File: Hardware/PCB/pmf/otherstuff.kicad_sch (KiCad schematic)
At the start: 65 parts, among them J10 Synth_power_2x5, J11 Conn_02x07_Odd_Even, J12 AudioJack2, J13 Conn_02x07_Odd_Even, J14 Conn_02x07_Odd_Even, J5 AudioJack2, J6 AudioJack2, J7 AudioJack2, J8 AudioJack2, J9 AudioJack2, SW1 SW_Rotary12, U2 TL072

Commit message: Rename libraries
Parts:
- C10, C11: footprint ao_tht:CP_Radial_D6.3mm_P2.50mm -> AO_tht:CP_Radial_D6.3mm_P2.50mm; symbol ao_symbols:CP -> AO_symbols:CP
- C12, C13: footprint ao_tht:C_Disc_D3.0mm_W1.6mm_P2.50mm -> AO_tht:C_Disc_D3.0mm_W1.6mm_P2.50mm; symbol ao_symbols:C -> AO_symbols:C
- D1, D2: footprint ao_tht:D_DO-41_SOD81_P10.16mm_Horizontal -> AO_tht:D_DO-41_SOD81_P10.16mm_Horizontal; symbol ao_symbols:1N5817 -> AO_symbols:1N5817
- GRAF1, GRAF2: symbol ao_symbols:Graphic -> AO_symbols:Graphic
- GRAF3: footprint ao_tht:analogoutput -> AO_tht:analogoutput; symbol ao_symbols:Graphic -> AO_symbols:Graphic
- H1, H2, H3: footprint ao_tht:MountingHole_3.2mm_M3 -> AO_tht:MountingHole_3.2mm_M3; symbol ao_symbols:MountingHole -> AO_symbols:MountingHole
- J10: footprint ao_tht:Power_Header -> AO_tht:Power_Header; symbol ao_symbols:Synth_power_2x5 -> AO_symbols:Synth_power_2x5
- J12, J5, J6, J7, J8, J9: footprint ao_tht:Jack_6.35mm_PJ_629HAN_slots -> AO_tht:Jack_6.35mm_PJ_629HAN_slots; symbol ao_symbols:AudioJack2 -> AO_symbols:AudioJack2
- R21, R22, R23, R24, R25, R26, R27, R28, R29, R31, R33, R34, R35, R36, R37, R38, R40, R42, R43, R47, R48, R49, R50, R51, R55, R56, R57, R58: footprint ao_tht:R_Axial_DIN0207_L6.3mm_D2.5mm_P10.16mm_Horizontal -> AO_tht:R_Axial_DIN0207_L6.3mm_D2.5mm_P10.16mm_Horizontal; symbol ao_symbols:R -> AO_symbols:R
- R30, R32, R39, R41, R44, R45, R46, R52, R53, R54: symbol ao_symbols:R -> AO_symbols:R
- SW1: footprint ao_tht:Rotary_Switch -> AO_tht:Rotary_Switch; symbol ao_symbols:SW_Rotary12 -> AO_symbols:SW_Rotary12
- TP7, TP8, TP9: footprint ao_tht:TestPoint_THTPad_D1.5mm_Drill0.7mm -> AO_tht:TestPoint_THTPad_D1.5mm_Drill0.7mm; symbol ao_symbols:TestPoint -> AO_symbols:TestPoint
- U2: footprint ao_tht:DIP-8_W7.62mm_Socket_LongPads -> AO_tht:DIP-8_W7.62mm_Socket_LongPads; symbol ao_symbols:TL072 -> AO_symbols:TL072

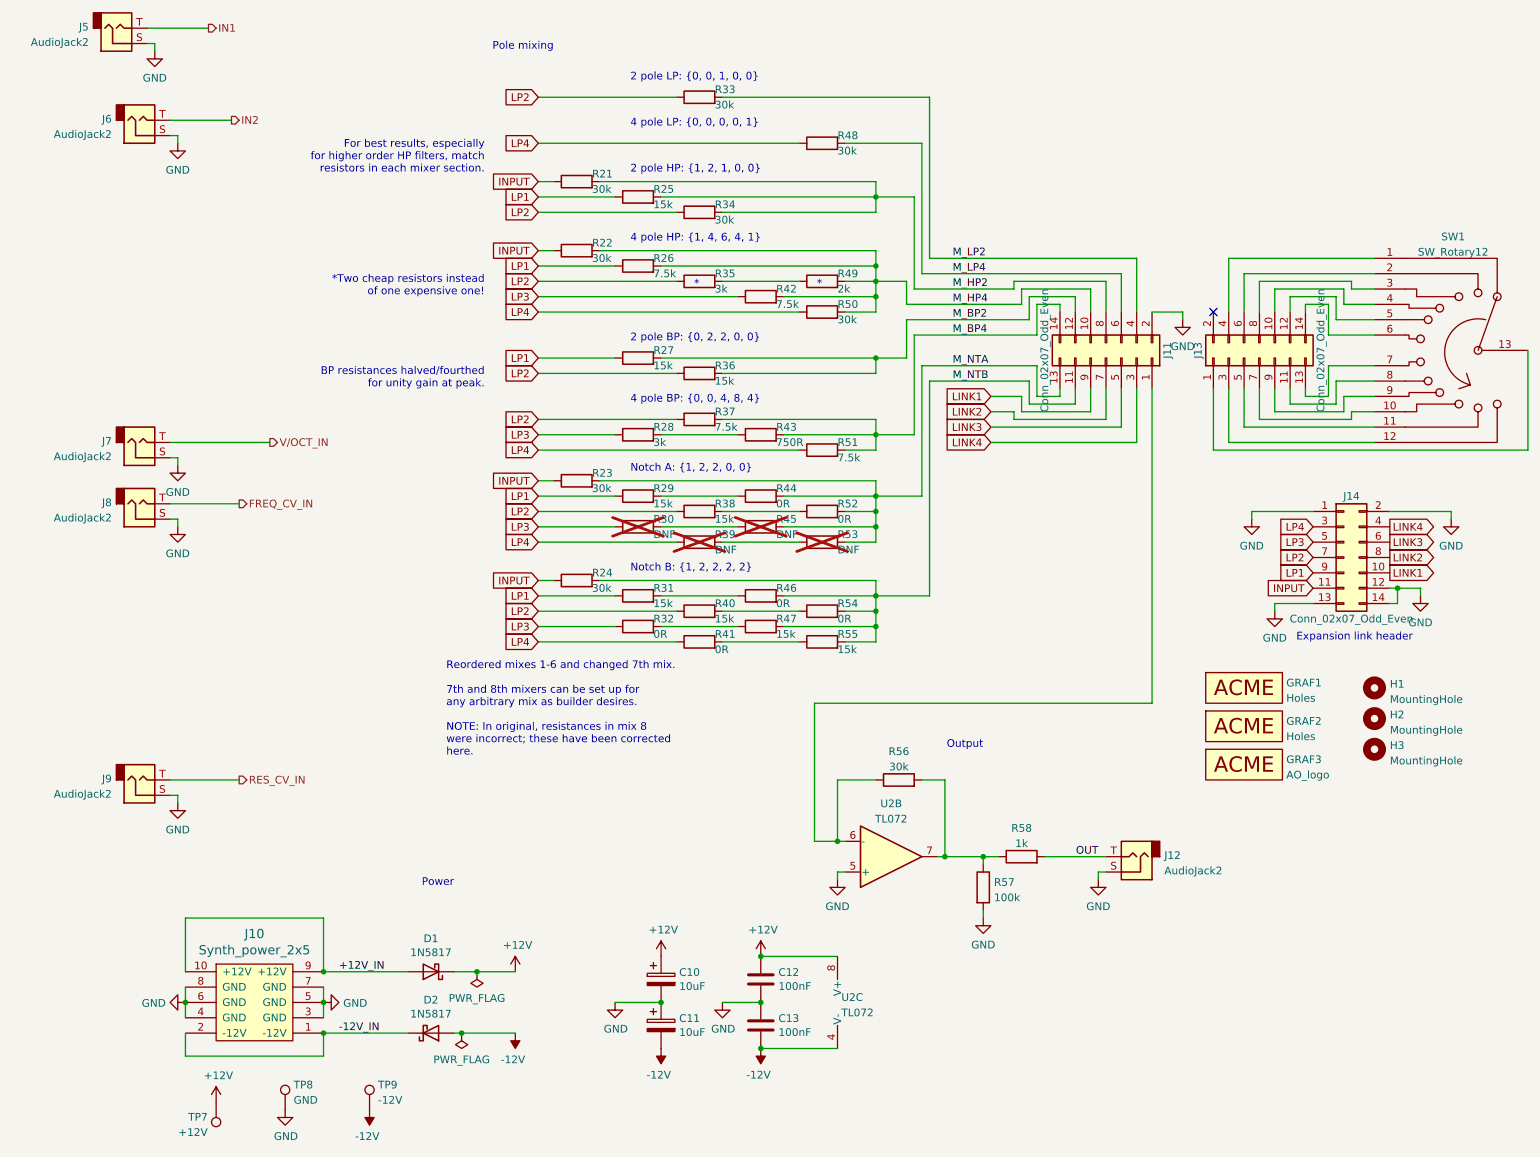
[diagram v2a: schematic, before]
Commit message: Remove VRES bias
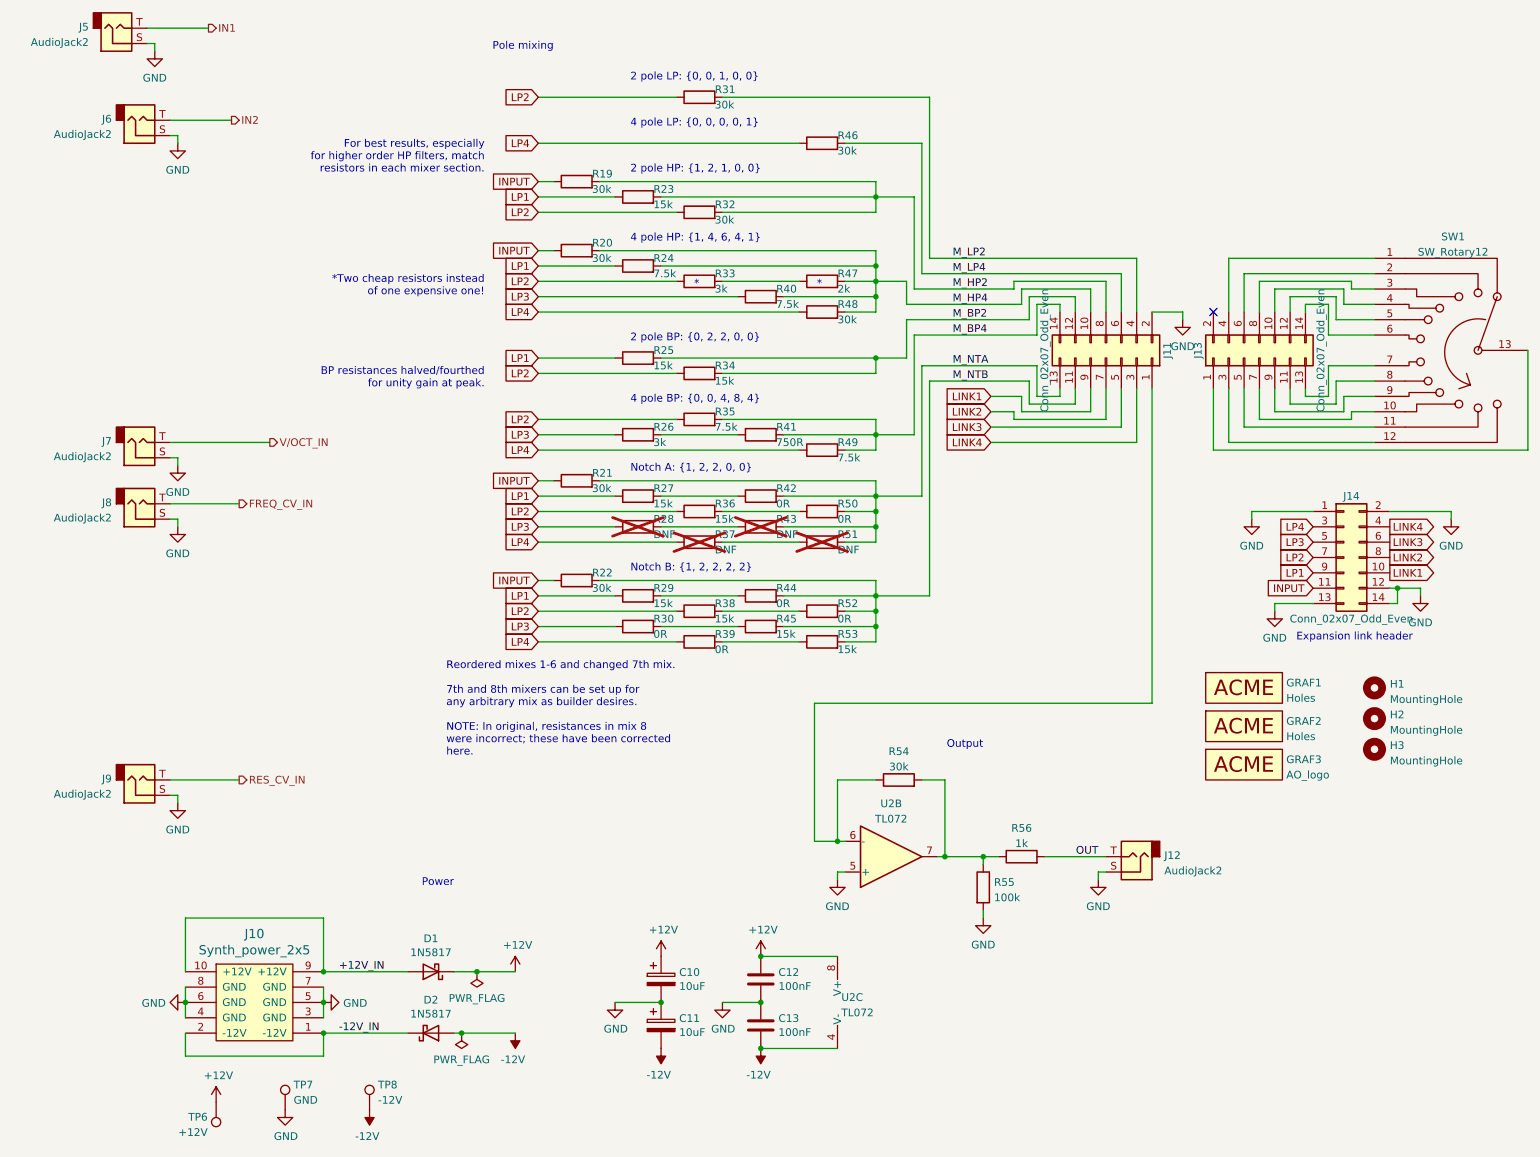
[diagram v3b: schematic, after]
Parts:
- renumbered R21 to R19, R22 to R20, R23 to R21, R24 to R22, R25 to R23, R26 to R24, R27 to R25, R28 to R26, R29 to R27, R30 to R28, R31 to R29, R32 to R30, R33 to R31, R34 to R32, R35 to R33, R36 to R34, R37 to R35, R38 to R36, R39 to R37, R40 to R38, R41 to R39, R42 to R40, R43 to R41, R44 to R42, R45 to R43, R46 to R44, R47 to R45, R48 to R46, R49 to R47, R50 to R48, R51 to R49, R52 to R50, R53 to R51, R54 to R52, R55 to R53, R56 to R54, R57 to R55, R58 to R56, TP7 to TP6, TP8 to TP7, TP9 to TP8

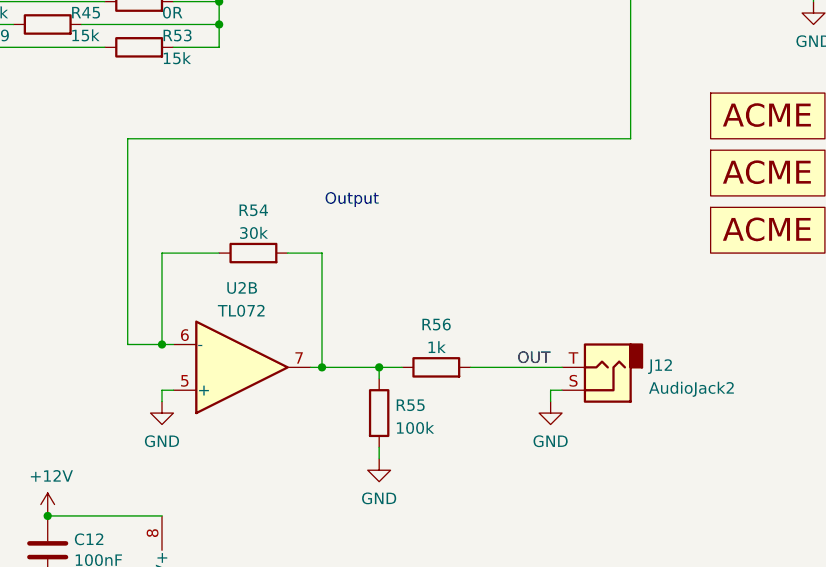
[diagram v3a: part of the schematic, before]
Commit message: Reduce amplitude at input and restore at output
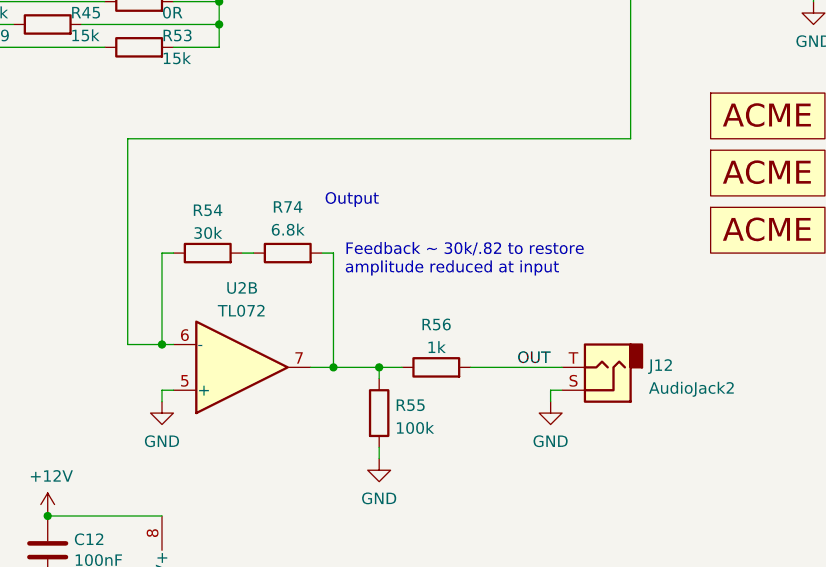
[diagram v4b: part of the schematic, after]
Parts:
- added R74: 6.8k, AO_tht:R_Axial_DIN0207_L6.3mm_D2.5mm_P10.16mm_Horizontal, symbol AO_symbols:R
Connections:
- net at R55.1, R56.1, U2.7: now also R74.2; no longer R54.2
- new net: R54.2, R74.1
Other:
- note added: "Feedback ~ 30k/.82 to restore amplitude reduced at input"
- moved on the sheet: R54
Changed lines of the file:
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@@
   (junction (at 154.94 100.33) (diameter 0) (color 0 0 0 0)
   )
-  (junction (at 166.37 154.94) (diameter 0) (color 0 0 0 0)
-  )
   (junction (at 154.94 111.76) (diameter 0) (color 0 0 0 0)
   )
@@
   (junction (at 63.5 173.99) (diameter 0) (color 0 0 0 0)
   )
+  (junction (at 167.64 154.94) (diameter 0) (color 0 0 0 0)
+  )
   (junction (at 154.94 45.72) (diameter 0) (color 0 0 0 0)
   )
@@
     (stroke (width 0) (type default))
   )
+  (wire (pts (xy 167.64 154.94) (xy 172.72 154.94))
+    (stroke (width 0) (type default))
+  )
   (wire (pts (xy 172.72 154.94) (xy 172.72 156.21))
     (stroke (width 0) (type default))
@@
     (stroke (width 0) (type default))
   )
-  (wire (pts (xy 166.37 154.94) (xy 172.72 154.94))
+  (wire (pts (xy 165.1 154.94) (xy 167.64 154.94))
     (stroke (width 0) (type default))
   )
@@
     (stroke (width 0) (type default))
   )
+  (wire (pts (xy 166.37 142.24) (xy 167.64 142.24))
+    (stroke (width 0) (type default))
+  )
   (wire (pts (xy 229.87 73.66) (xy 229.87 78.74))
     (stroke (width 0) (type default))
@@
     (stroke (width 0) (type default))
   )
-  (wire (pts (xy 148.59 142.24) (xy 154.94 142.24))
+  (wire (pts (xy 148.59 142.24) (xy 149.86 142.24))
     (stroke (width 0) (type default))
   )
@@
     (stroke (width 0) (type default))
   )
-  (wire (pts (xy 166.37 154.94) (xy 165.1 154.94))
-    (stroke (width 0) (type default))
-  )
   (wire (pts (xy 173.99 81.28) (xy 177.8 81.28))
     (stroke (width 0) (type default))
@@
     (stroke (width 0) (type default))
   )
-  (wire (pts (xy 166.37 142.24) (xy 166.37 154.94))
+  (wire (pts (xy 167.64 142.24) (xy 167.64 154.94))
     (stroke (width 0) (type default))
   )
@@
     (stroke (width 0) (type default))
   )
-  (wire (pts (xy 162.56 142.24) (xy 166.37 142.24))
+  (wire (pts (xy 157.48 142.24) (xy 158.75 142.24))
     (stroke (width 0) (type default))
   )
@@
     (effects (font (size 1.27 1.27)) (justify left bottom))
   )
+  (text "Feedback ~ 30k/.82 to restore\namplitude reduced at input"
+    (at 168.91 144.78 0)
+    (effects (font (size 1.27 1.27)) (justify left bottom))
+  )
   (text "2 pole HP: {1, 2, 1, 0, 0}" (at 114.3 41.91 0)
     (effects (font (size 1.27 1.27)) (justify left bottom))
@@
     )
   )
-  (symbol (lib_id "AO_symbols:R") (at 158.75 142.24 90) (unit 1)
+  (symbol (lib_id "AO_symbols:R") (at 153.67 142.24 90) (unit 1)
     (in_bom yes) (on_board yes) (dnp no) (fields_autoplaced)
-    (property "Reference" "R54" (at 158.75 137.5242 90)
+    (property "Reference" "R54" (at 153.67 137.5242 90)
       (effects (font (size 1.27 1.27)))
     )
-    (property "Value" "30k" (at 158.75 140.0611 90)
+    (property "Value" "30k" (at 153.67 140.0611 90)
       (effects (font (size 1.27 1.27)))
     )
-    (property "Footprint" "AO_tht:R_Axial_DIN0207_L6.3mm_D2.5mm_P10.16mm_Horizontal" (at 158.75 144.018 90)
+    (property "Footprint" "AO_tht:R_Axial_DIN0207_L6.3mm_D2.5mm_P10.16mm_Horizontal" (at 153.67 144.018 90)
       (effects (font (size 1.27 1.27)) hide)
     )
-    (property "Datasheet" "" (at 158.75 142.24 0)
+    (property "Datasheet" "" (at 153.67 142.24 0)
       (effects (font (size 1.27 1.27)) hide)
     )
-    (property "Vendor" "Tayda" (at 158.75 142.24 0)
+    (property "Vendor" "Tayda" (at 153.67 142.24 0)
       (effects (font (size 1.27 1.27)) hide)
     )
@@
         )
       )
+    )
+  )
+  (symbol (lib_id "AO_symbols:R") (at 162.56 142.24 90) (unit 1)
+    (in_bom yes) (on_board yes) (dnp no) (fields_autoplaced)
+    (property "Reference" "R74" (at 162.56 137.16 90)
+      (effects (font (size 1.27 1.27)))
+    )
+    (property "Value" "6.8k" (at 162.56 139.7 90)
+      (effects (font (size 1.27 1.27)))
+    )
+    (property "Footprint" "AO_tht:R_Axial_DIN0207_L6.3mm_D2.5mm_P10.16mm_Horizontal" (at 162.56 144.018 90)
+      (effects (font (size 1.27 1.27)) hide)
+    )
+    (property "Datasheet" "" (at 162.56 142.24 0)
+      (effects (font (size 1.27 1.27)) hide)
+    )
+    (property "Vendor" "Tayda" (at 162.56 142.24 0)
+      (effects (font (size 1.27 1.27)) hide)
+    )
+    (pin "1")
+    (pin "2")
+    (instances
+      (project "pmf"
+        (path "/1fce46f5-2003-4c7e-915f-b9b7dfc679d7/a180c6ca-d86a-4fef-be09-a6b0b94046eb"
+          (reference "R74") (unit 1)
+        )
+      )

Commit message: Large attenuation and amplification
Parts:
- R74: value 6.8k -> 30k
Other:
- note added: "Feedback 30k x 2 to restore amplitude reduced at input"
- note removed: "Feedback ~ 30k/.82 to restore amplitude reduced at input"
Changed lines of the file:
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@@
     (effects (font (size 1.27 1.27)) (justify left bottom))
   )
-  (text "Feedback ~ 30k/.82 to restore\namplitude reduced at input"
+  (text "Feedback 30k x 2 to restore\namplitude reduced at input"
     (at 168.91 144.78 0)
     (effects (font (size 1.27 1.27)) (justify left bottom))
@@
       (effects (font (size 1.27 1.27)))
     )
-    (property "Value" "6.8k" (at 162.56 139.7 90)
-      (effects (font (size 1.27 1.27)))
-    )
+    (property "Value" "30k" (at 162.56 139.7 90)
+      (effects (font (size 1.27 1.27)))
+    )
